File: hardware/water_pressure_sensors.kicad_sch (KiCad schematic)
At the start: 0 parts

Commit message: Add the Cube project
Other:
- title: Water Pressure Sensor -> Water Pressure Sensors
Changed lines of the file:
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@@
   (paper "A4")
   (title_block
-    (title "Water Pressure Sensor")
-    (date "2023-06-06")
+    (title "Water Pressure Sensors")
+    (date "2023-07-01")
     (rev "${REVISION}")
     (company "Author: I. Kajdan")

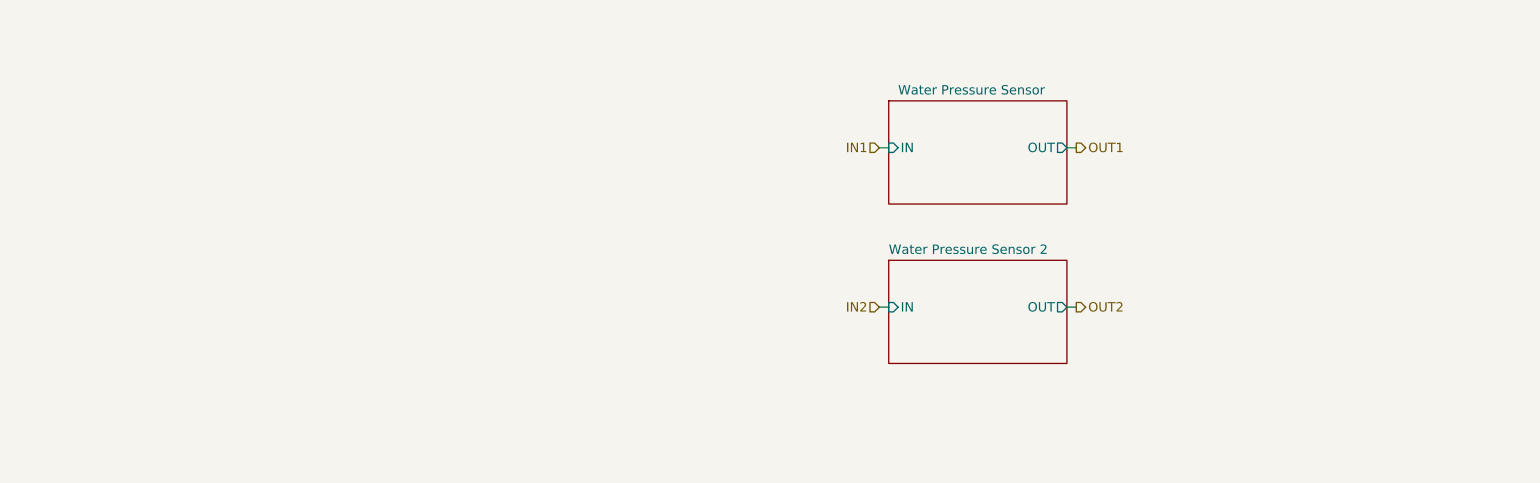
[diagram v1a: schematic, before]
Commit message: Improve the schematic
- add anti-aliasing filters
- rearrange the main connector signals
- improve the power filtering
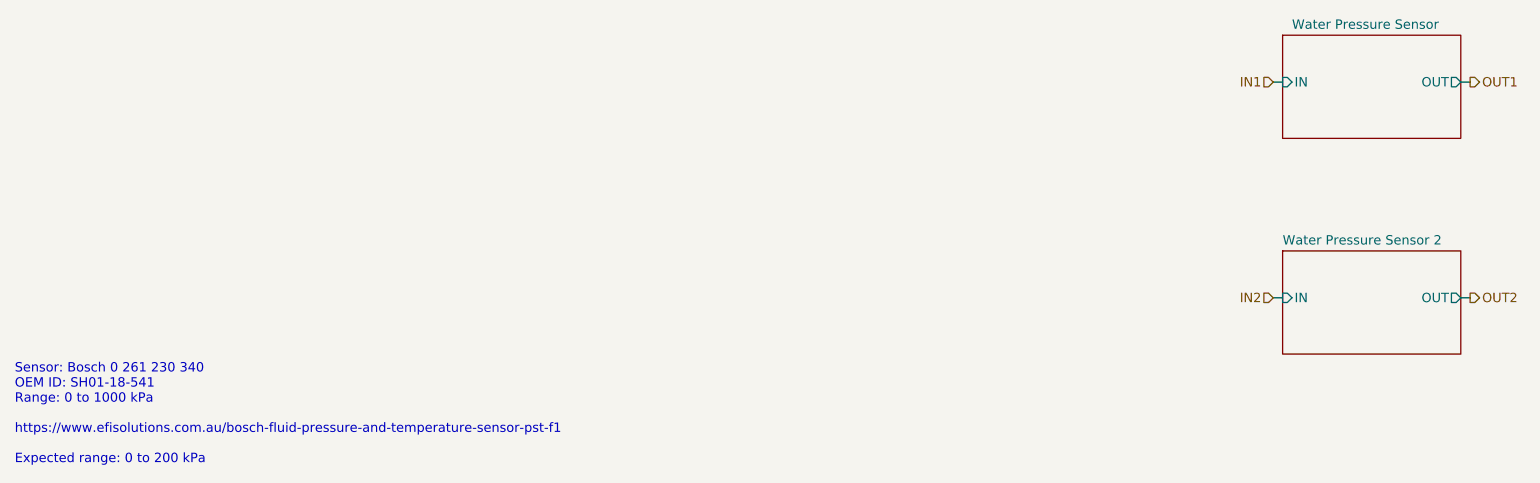
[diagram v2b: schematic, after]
